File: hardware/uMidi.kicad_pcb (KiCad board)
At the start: 2 copper layers, 66 x 40.6 mm, 65 parts, among them CON1 USB-MINI-B, IC1 ATXMEGA128A4U-M, IC2 74LS14, IC3 LT1129CST-3.3, IC4 6N138, P1 MIDI In, P2 MIDI Thru, P3 MIDI T/O, P4 MIDI Out, P5 5..12 V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

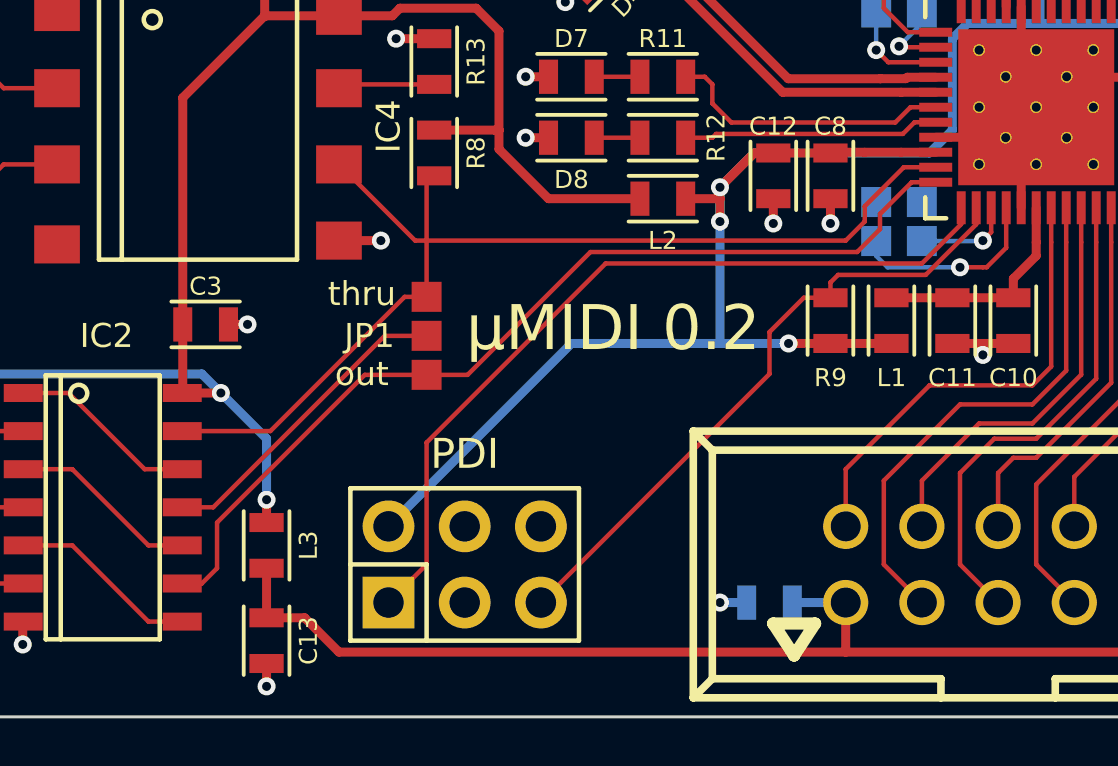
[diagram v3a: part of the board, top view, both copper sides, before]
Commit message: Optimize jumper placement
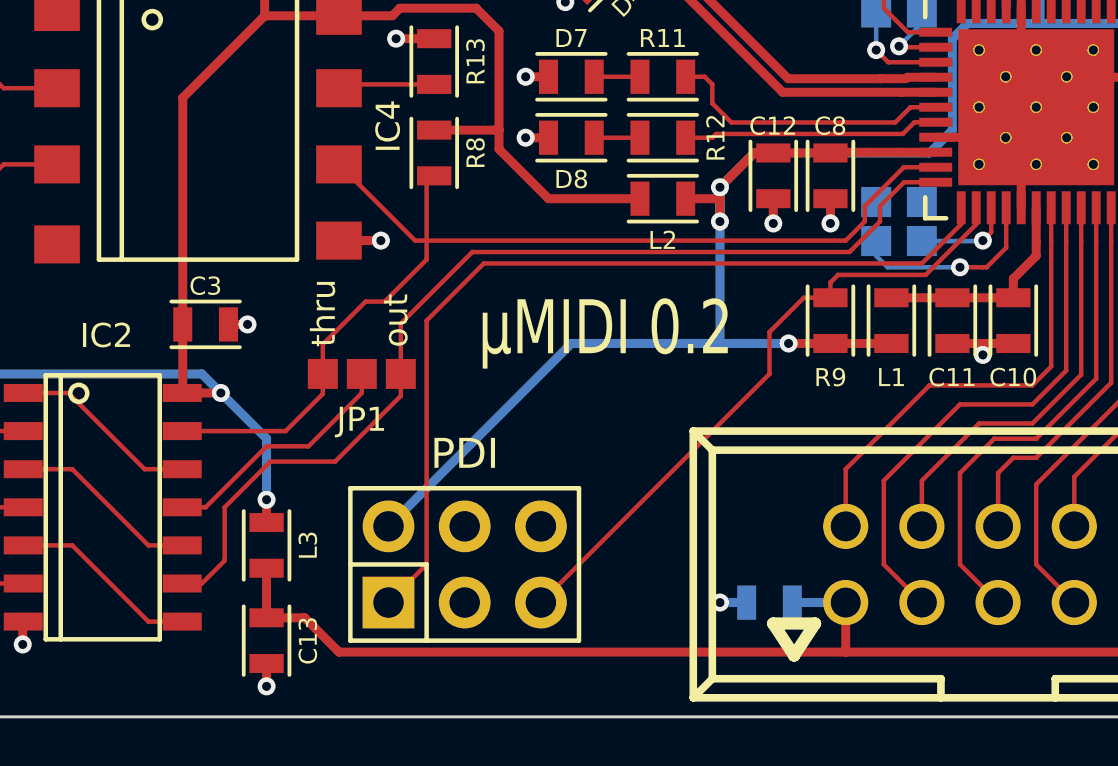
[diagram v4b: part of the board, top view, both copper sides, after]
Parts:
- moved JP1 2.50 mm to (91.8, 152.4), turned to 0 degrees
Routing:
- net Net-(IC1-Pad34): track 27.2 -> 29.6 mm
- net Net-(IC2-Pad11): track 10.5 -> 8.20 mm
- net TXD: track 31.8 -> 33.4 mm
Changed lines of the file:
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@@
     (thickness 1.6)
     (drawings 26)
-    (tracks 530)
+    (tracks 538)
     (zones 0)
     (modules 65)
@@
   )
   (module Solderjumper:SJ3 placed (layer F.Cu)
-    (at 93.98 151.13 270)
-    (fp_text reference JP1 (at 0 1.905 360) (layer F.SilkS)
+    (at 91.821 152.4)
+    (fp_text reference JP1 (at 0 1.524 180) (layer F.SilkS)
       (effects (font (size 0.8 0.8) (thickness 0.15)))
     )
-    (fp_text value JUMPER3 (at 0 2.54 270) (layer F.SilkS) hide
+    (fp_text value JUMPER3 (at 0 2.54) (layer F.SilkS) hide
       (effects (font (size 1.5 1.5) (thickness 0.15)))
     )
-    (pad 2 smd rect (at 0 0 270) (size 1 1) (layers F.Cu F.Paste F.Mask)
+    (pad 2 smd rect (at 0 0) (size 1 1) (layers F.Cu F.Paste F.Mask)
       (net 67 "Net-(IC2-Pad11)") (solder_mask_margin 0.2))
-    (pad 1 smd rect (at -1.3 0 270) (size 1 1) (layers F.Cu F.Paste F.Mask)
+    (pad 1 smd rect (at -1.3 0) (size 1 1) (layers F.Cu F.Paste F.Mask)
       (net 12 RXD) (solder_mask_margin 0.2))
-    (pad 3 smd rect (at 1.3 0 270) (size 1 1) (layers F.Cu F.Paste F.Mask)
+    (pad 3 smd rect (at 1.3 0) (size 1 1) (layers F.Cu F.Paste F.Mask)
       (net 34 TXD) (solder_mask_margin 0.2))
   )
@@
     (effects (font (size 0.6 0.6) (thickness 0.12)))
   )
-  (gr_text "µMIDI 0.2" (at 100.203 150.876) (layer F.SilkS)
-    (effects (font (size 1.5 1.5) (thickness 0.15)))
-  )
-  (gr_text out (at 91.821 152.4) (layer F.SilkS)
+  (gr_text "µMIDI 0.2" (at 99.949 150.876) (layer F.SilkS)
+    (effects (font (size 1.8 1.3) (thickness 0.15)))
+  )
+  (gr_text out (at 92.964 150.622 90) (layer F.SilkS)
     (effects (font (size 0.8 0.8) (thickness 0.15)))
   )
-  (gr_text thru (at 91.821 149.733) (layer F.SilkS)
+  (gr_text thru (at 90.551 150.368 90) (layer F.SilkS)
     (effects (font (size 0.8 0.8) (thickness 0.15)))
   )
@@
   (segment (start 77.47 141.478) (end 78.232 140.716) (width 0.15) (layer F.Cu) (net 11))
   (segment (start 77.47 142.24508) (end 77.47 141.478) (width 0.15) (layer F.Cu) (net 11))
+  (segment (start 90.521 152.4) (end 90.521 151.414) (width 0.15) (layer F.Cu) (net 12))
+  (segment (start 93.98 148.59) (end 93.98 147.955) (width 0.15) (layer F.Cu) (net 12))
+  (segment (start 92.583 149.987) (end 93.98 148.59) (width 0.15) (layer F.Cu) (net 12))
+  (segment (start 91.948 149.987) (end 92.583 149.987) (width 0.15) (layer F.Cu) (net 12))
+  (segment (start 90.521 151.414) (end 91.948 149.987) (width 0.15) (layer F.Cu) (net 12))
+  (segment (start 85.835 154.305) (end 89.281 154.305) (width 0.15) (layer F.Cu) (net 12))
+  (segment (start 90.521 153.065) (end 90.521 152.4) (width 0.15) (layer F.Cu) (net 12))
+  (segment (start 89.281 154.305) (end 90.521 153.065) (width 0.15) (layer F.Cu) (net 12))
   (segment (start 110.95 145.51) (end 109.887 145.51) (width 0.15) (layer F.Cu) (net 12))
+  (segment (start 109.887 145.51) (end 108.585 146.812) (width 0.15) (layer F.Cu) (net 12))
+  (segment (start 108.585 146.812) (end 108.585 147.32) (width 0.15) (layer F.Cu) (net 12))
+  (segment (start 108.585 147.32) (end 107.95 147.955) (width 0.15) (layer F.Cu) (net 12))
   (segment (start 107.95 147.955) (end 93.98 147.955) (width 0.15) (layer F.Cu) (net 12))
-  (segment (start 108.585 147.32) (end 107.95 147.955) (width 0.15) (layer F.Cu) (net 12))
-  (segment (start 108.585 146.812) (end 108.585 147.32) (width 0.15) (layer F.Cu) (net 12))
-  (segment (start 109.887 145.51) (end 108.585 146.812) (width 0.15) (layer F.Cu) (net 12))
   (segment (start 94.234 145.796) (end 93.98 146.05) (width 0.15) (layer F.Cu) (net 12))
   (segment (start 93.98 146.05) (end 93.98 147.955) (width 0.15) (layer F.Cu) (net 12))
   (segment (start 91.059 145.415) (end 93.599 147.955) (width 0.15) (layer F.Cu) (net 12))
   (segment (start 93.599 147.955) (end 93.98 147.955) (width 0.15) (layer F.Cu) (net 12))
-  (segment (start 93.98 147.955) (end 93.98 149.83) (width 0.15) (layer F.Cu) (net 12))
-  (segment (start 88.773 154.305) (end 93.248 149.83) (width 0.15) (layer F.Cu) (net 12))
-  (segment (start 93.248 149.83) (end 93.98 149.83) (width 0.15) (layer F.Cu) (net 12))
-  (segment (start 85.835 154.305) (end 88.773 154.305) (width 0.15) (layer F.Cu) (net 12))
   (segment (start 117.65 146.01) (end 118.832 146.01) (width 0.15) (layer F.Cu) (net 13))
   (segment (start 114.3 158.75) (end 115.57 160.02) (width 0.15) (layer F.Cu) (net 13))
@@
   (segment (start 103.505 144.526) (end 102.616 144.526) (width 0.15) (layer F.Cu) (net 33))
   (segment (start 110.95 144.01) (end 110.244 144.01) (width 0.15) (layer F.Cu) (net 33))
-  (segment (start 110.95 146.01) (end 110.149 146.01) (width 0.15) (layer F.Cu) (net 34))
-  (segment (start 95.347 152.43) (end 93.98 152.43) (width 0.15) (layer F.Cu) (net 34))
-  (segment (start 99.441 148.336) (end 95.347 152.43) (width 0.15) (layer F.Cu) (net 34))
-  (segment (start 108.331 148.336) (end 99.441 148.336) (width 0.15) (layer F.Cu) (net 34))
-  (segment (start 109.093 147.574) (end 108.331 148.336) (width 0.15) (layer F.Cu) (net 34))
-  (segment (start 109.093 147.066) (end 109.093 147.574) (width 0.15) (layer F.Cu) (net 34))
-  (segment (start 110.149 146.01) (end 109.093 147.066) (width 0.15) (layer F.Cu) (net 34))
-  (segment (start 86.487 159.385) (end 86.995 158.877) (width 0.15) (layer F.Cu) (net 34))
-  (segment (start 86.995 158.877) (end 86.995 157.353) (width 0.15) (layer F.Cu) (net 34))
-  (segment (start 86.995 157.353) (end 91.918 152.43) (width 0.15) (layer F.Cu) (net 34))
-  (segment (start 91.918 152.43) (end 93.98 152.43) (width 0.15) (layer F.Cu) (net 34))
+  (segment (start 110.95 146.01) (end 109.895 146.01) (width 0.15) (layer F.Cu) (net 34))
+  (segment (start 93.121 150.719) (end 93.121 152.4) (width 0.15) (layer F.Cu) (net 34))
+  (segment (start 95.504 148.336) (end 93.121 150.719) (width 0.15) (layer F.Cu) (net 34))
+  (segment (start 108.077 148.336) (end 95.504 148.336) (width 0.15) (layer F.Cu) (net 34))
+  (segment (start 109.093 147.32) (end 108.077 148.336) (width 0.15) (layer F.Cu) (net 34))
+  (segment (start 109.093 146.812) (end 109.093 147.32) (width 0.15) (layer F.Cu) (net 34))
+  (segment (start 109.895 146.01) (end 109.093 146.812) (width 0.15) (layer F.Cu) (net 34))
   (segment (start 85.835 159.385) (end 86.487 159.385) (width 0.15) (layer F.Cu) (net 34))
-  (segment (start 93.98 158.75) (end 93.98 154.686) (width 0.15) (layer F.Cu) (net 35))
-  (segment (start 93.98 154.686) (end 99.949 148.717) (width 0.15) (layer F.Cu) (net 35))
-  (segment (start 99.949 148.717) (end 110.49 148.717) (width 0.15) (layer F.Cu) (net 35))
+  (segment (start 93.121 153.132) (end 93.121 152.4) (width 0.15) (layer F.Cu) (net 34))
+  (segment (start 90.932 155.321) (end 93.121 153.132) (width 0.15) (layer F.Cu) (net 34))
+  (segment (start 88.773 155.321) (end 90.932 155.321) (width 0.15) (layer F.Cu) (net 34))
+  (segment (start 87.249 156.845) (end 88.773 155.321) (width 0.15) (layer F.Cu) (net 34))
+  (segment (start 87.249 158.623) (end 87.249 156.845) (width 0.15) (layer F.Cu) (net 34))
+  (segment (start 86.487 159.385) (end 87.249 158.623) (width 0.15) (layer F.Cu) (net 34))
+  (segment (start 93.98 158.75) (end 93.98 150.622) (width 0.15) (layer F.Cu) (net 35))
+  (segment (start 93.98 150.622) (end 95.885 148.717) (width 0.15) (layer F.Cu) (net 35))
+  (segment (start 95.885 148.717) (end 110.49 148.717) (width 0.15) (layer F.Cu) (net 35))
   (segment (start 110.49 148.717) (end 111.8 147.407) (width 0.15) (layer F.Cu) (net 35))
   (segment (start 111.8 147.407) (end 111.8 146.86) (width 0.15) (layer F.Cu) (net 35))
@@
   (segment (start 78.74 161.29) (end 78.232 161.29) (width 0.15) (layer F.Cu) (net 66))
   (segment (start 80.535 159.385) (end 79.502 159.385) (width 0.15) (layer F.Cu) (net 66))
-  (segment (start 86.868 156.845) (end 92.583 151.13) (width 0.15) (layer F.Cu) (net 67))
-  (segment (start 92.583 151.13) (end 93.98 151.13) (width 0.15) (layer F.Cu) (net 67))
-  (segment (start 85.835 156.845) (end 86.868 156.845) (width 0.15) (layer F.Cu) (net 67))
+  (segment (start 85.835 156.845) (end 86.614 156.845) (width 0.15) (layer F.Cu) (net 67))
+  (segment (start 91.821 153.035) (end 91.821 152.4) (width 0.15) (layer F.Cu) (net 67))
+  (segment (start 90.043 154.813) (end 91.821 153.035) (width 0.15) (layer F.Cu) (net 67))
+  (segment (start 88.646 154.813) (end 90.043 154.813) (width 0.15) (layer F.Cu) (net 67))
+  (segment (start 86.614 156.845) (end 88.646 154.813) (width 0.15) (layer F.Cu) (net 67))
   (segment (start 122.428 141.478) (end 122.428 140.843) (width 0.15) (layer F.Cu) (net 68))
   (segment (start 123.698 140.843) (end 126.365 143.51) (width 0.15) (layer F.Cu) (net 68))

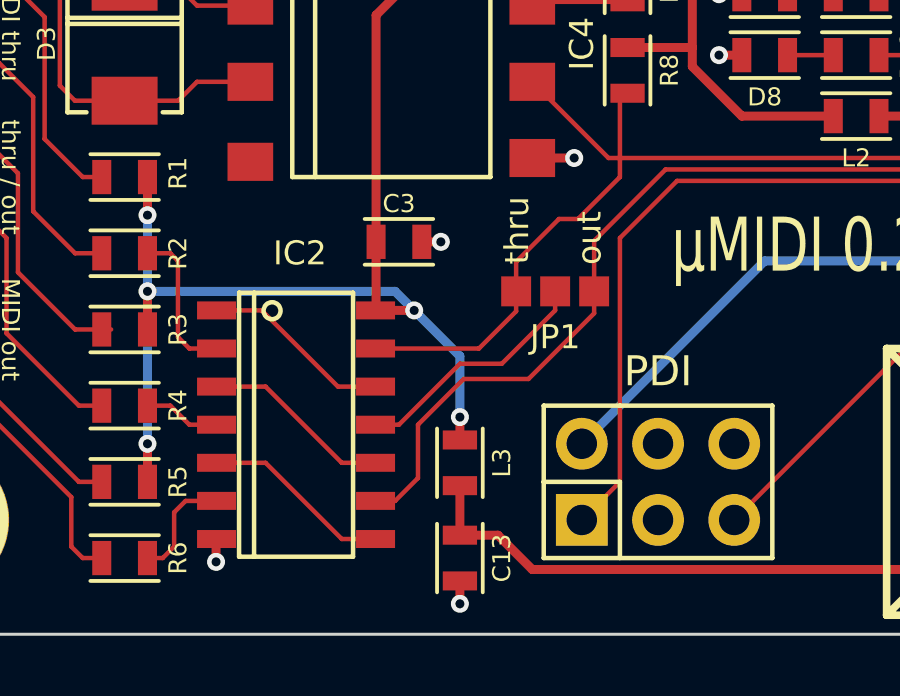
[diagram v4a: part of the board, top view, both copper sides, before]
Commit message: Optimize silkscreen
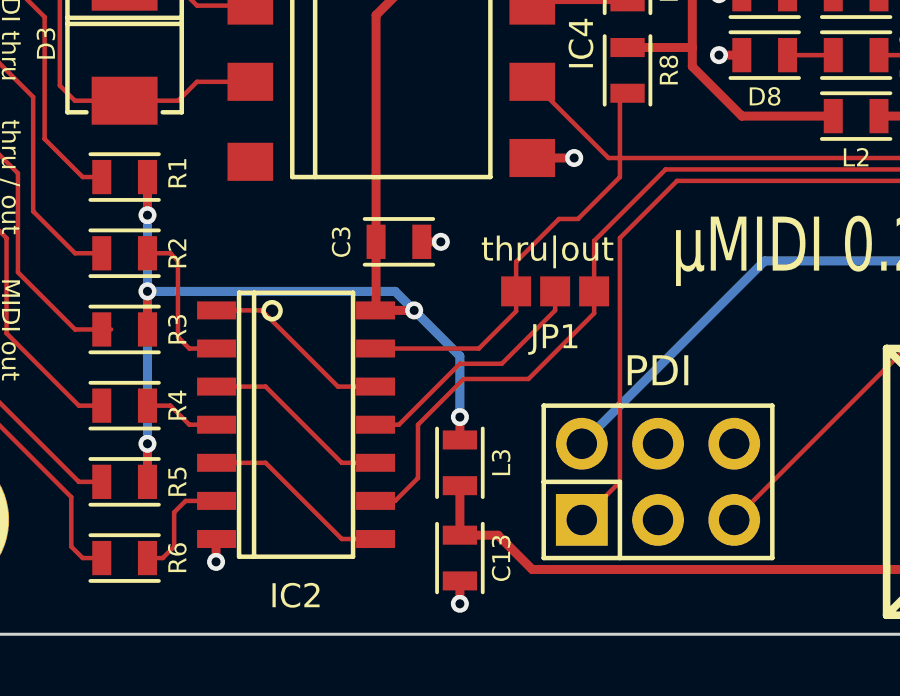
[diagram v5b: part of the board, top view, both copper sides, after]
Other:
- board text added: "thru|out"
- board text removed: "out"
- board text removed: "thru"
